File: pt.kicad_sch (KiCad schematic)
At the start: 13 parts, among them J9 PT

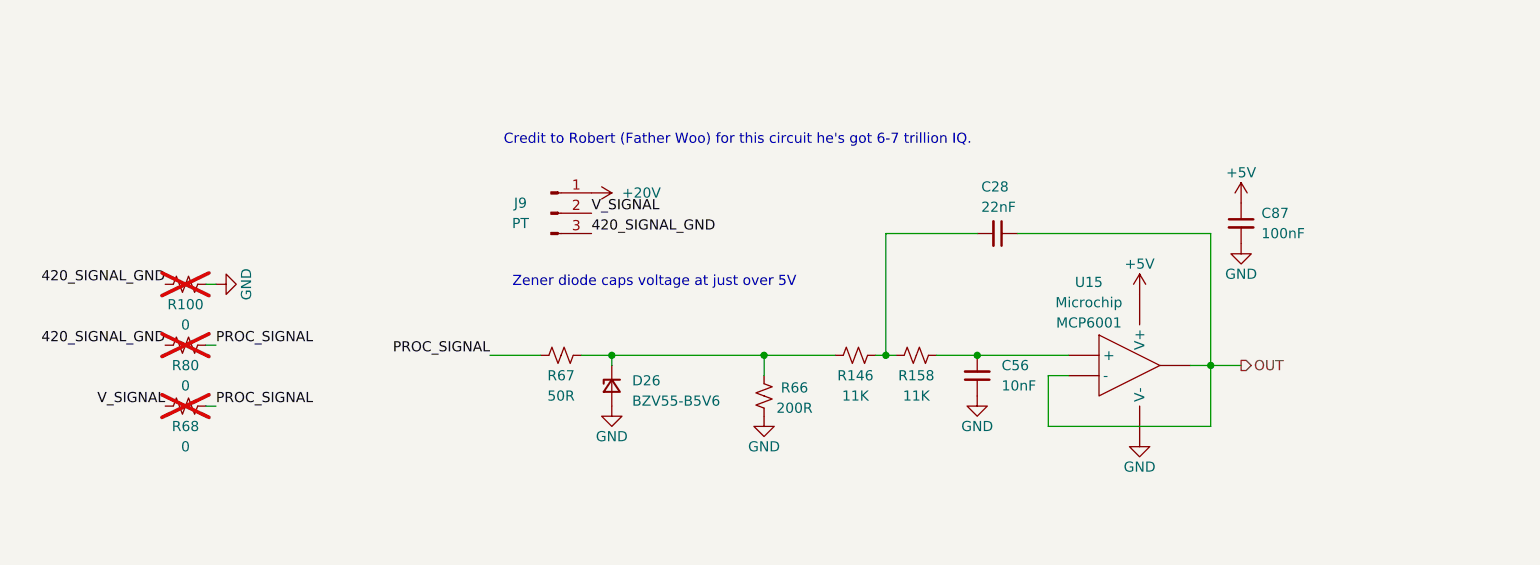
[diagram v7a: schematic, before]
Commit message: All on back + new circuit
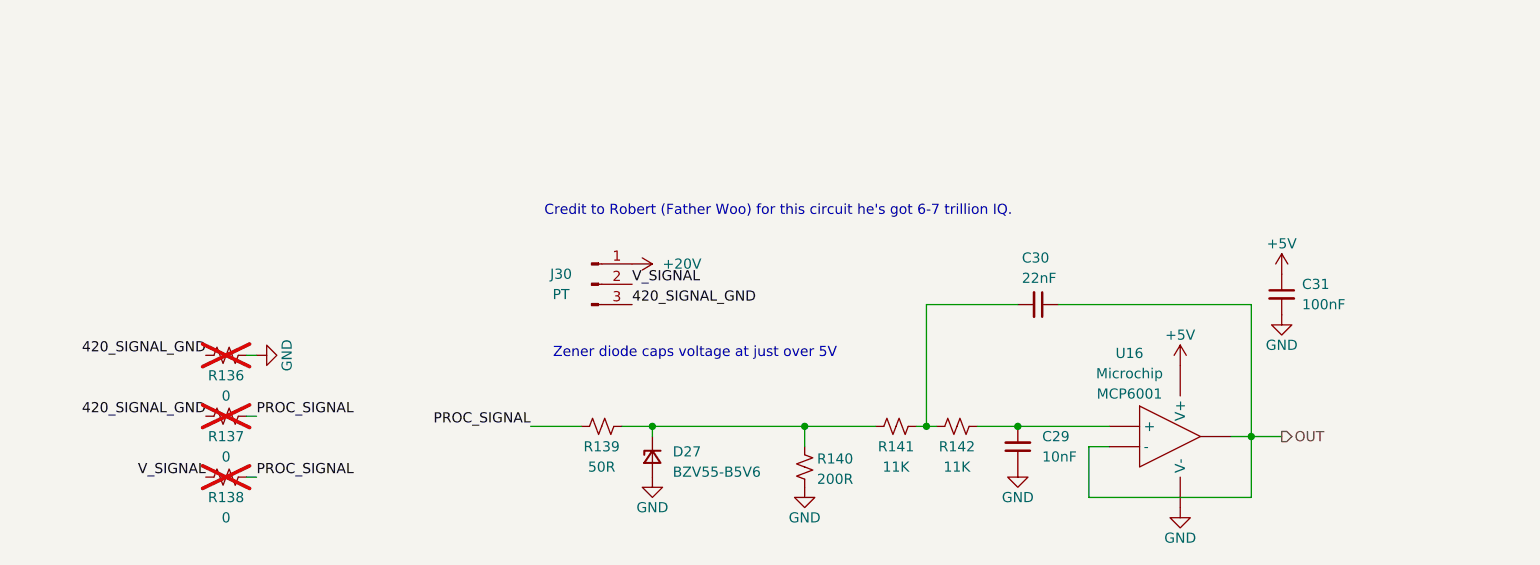
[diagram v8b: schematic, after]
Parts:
- removed C28: 22nF, Capacitor_SMD:C_0603_1608Metric, symbol Device:C_Small
- removed C56: 10nF, Capacitor_SMD:C_0603_1608Metric, symbol Device:C_Small
- removed C87: 100nF, Capacitor_SMD:C_0603_1608Metric, symbol Device:C_Small
- removed D26: BZV55-B5V6, Diode_SMD:D_MiniMELF, symbol UCIRP-KiCAD-Lib:D_Zener_Small
- removed J9: PT, 0UCIRP-KiCAD-Lib:GX-12 3 pin, symbol Connector:Conn_01x03_Pin
- removed R100, R68, R80: 0, Resistor_SMD:R_1210_3225Metric_Pad1.30x2.65mm_HandSolder, symbol Device:R_Small_US
- removed R146, R158: 11K, Resistor_SMD:R_0603_1608Metric, symbol Device:R_Small_US
- removed R66: 200R, Resistor_SMD:R_0603_1608Metric, symbol Device:R_Small_US
- removed R67: 50R, Resistor_SMD:R_0603_1608Metric, symbol Device:R_Small_US
- removed U15: ~, Package_TO_SOT_SMD:SOT-23-5, symbol UCIRP-KiCAD-Lib:MCP6001
- added C29: 10nF, Capacitor_SMD:C_0603_1608Metric, symbol Device:C_Small
- added C30: 22nF, Capacitor_SMD:C_0603_1608Metric, symbol Device:C_Small
- added C31: 100nF, Capacitor_SMD:C_0603_1608Metric, symbol Device:C_Small
- added D27: BZV55-B5V6, Diode_SMD:D_MiniMELF, symbol UCIRP-KiCAD-Lib:D_Zener_Small
- added J30: PT, 0UCIRP-KiCAD-Lib:GX-12 3 pin, symbol Connector:Conn_01x03_Pin
- added R136, R137, R138: 0, Resistor_SMD:R_1210_3225Metric_Pad1.30x2.65mm_HandSolder, symbol Device:R_Small_US
- added R139: 50R, Resistor_SMD:R_0603_1608Metric, symbol Device:R_Small_US
- added R140: 200R, Resistor_SMD:R_0603_1608Metric, symbol Device:R_Small_US
- added R141, R142: 11K, Resistor_SMD:R_0603_1608Metric, symbol Device:R_Small_US
- added U16: ~, Package_TO_SOT_SMD:SOT-23-5, symbol UCIRP-KiCAD-Lib:MCP6001
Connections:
- net +20V: now also J30.1 (Pin_1)
- net +5V: now also C31.1, U16.5 (V+)
- net 420_SIGNAL_GND: now also J30.3 (Pin_3), R136.2, R137.2
- net GND: now also C29.1, C31.2, D27.2 (A), R136.1, R140.1, U16.2 (V-)
- net OUT: now also C30.1, U16.1, U16.4 (-)
- net PROC_SIGNAL: now also R137.1, R138.1, R139.2
- net V_SIGNAL: now also J30.2 (Pin_2), R138.2
- new net: D27.1 (K), R139.1, R140.2, R141.2
- new net: C29.2, R142.1, U16.3 (+)
- new net: C30.2, R141.1, R142.2
